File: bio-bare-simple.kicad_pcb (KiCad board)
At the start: 2 copper layers, 49.7 x 49.7 mm, 6 parts, among them X1 Badgelife_shitty_connector

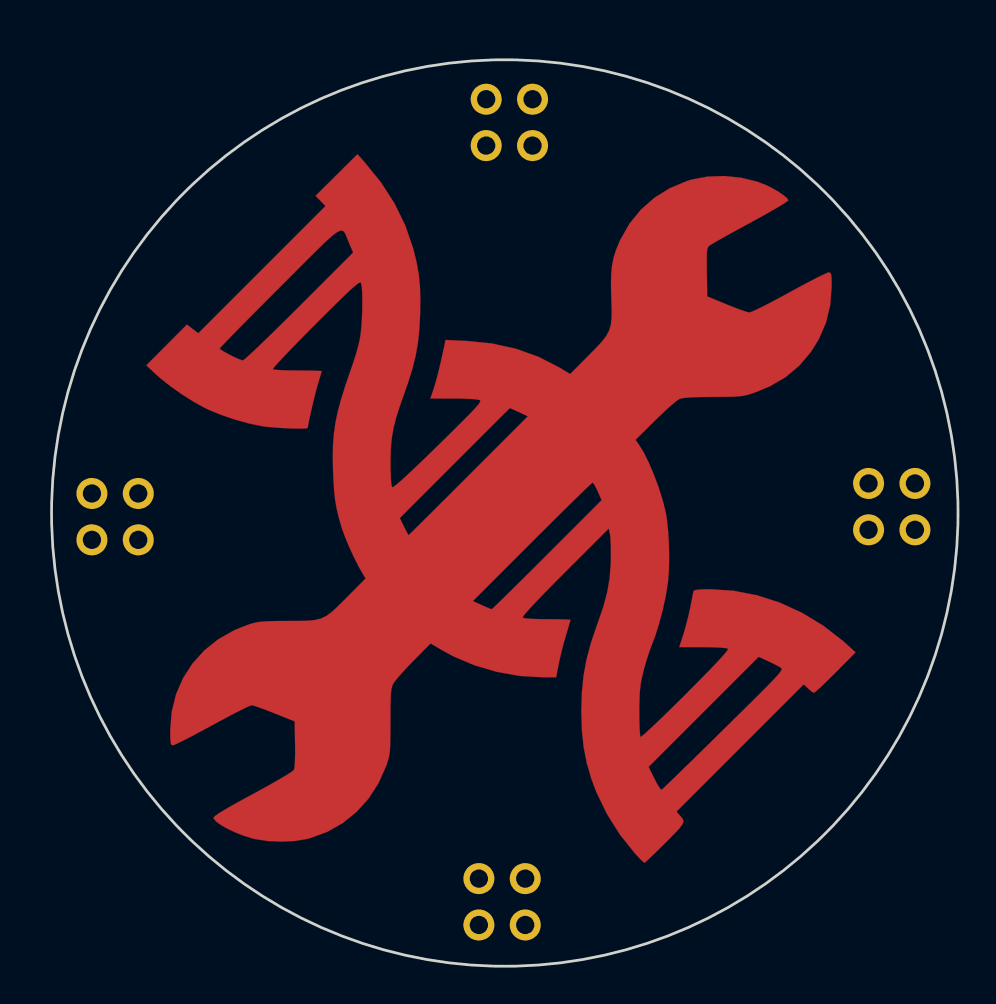
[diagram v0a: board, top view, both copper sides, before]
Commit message: add simple BioHacking Village artwork to add-on board
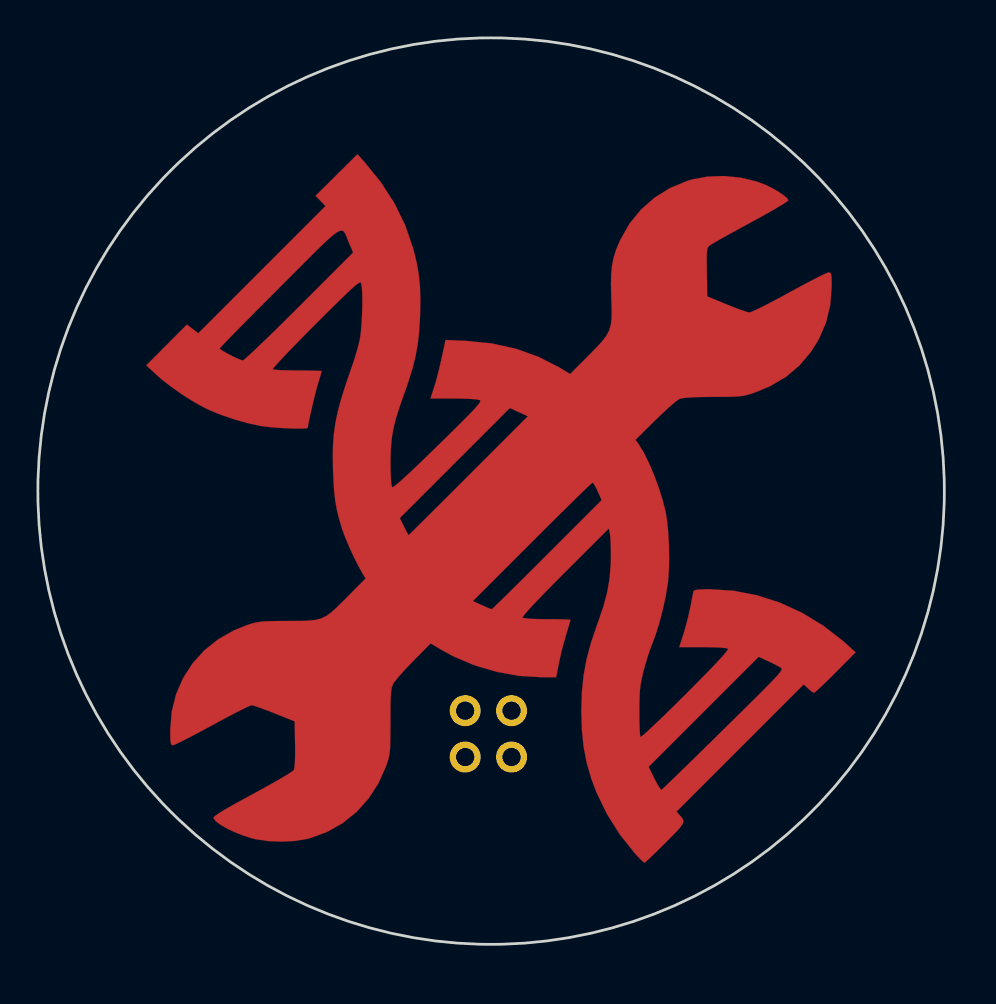
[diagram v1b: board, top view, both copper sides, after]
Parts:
- removed the X1 at (147.3, 135.8)
- removed the X1 at (168.3, 156.8)
- removed the X1 at (125.8, 157.3)
- moved X1 9.23 mm to (146.2, 169.2)
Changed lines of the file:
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@@
 (kicad_pcb (version 4) (host pcbnew 4.0.6+dfsg1-1)
   (general
-    (links 12)
-    (no_connects 12)
+    (links 0)
+    (no_connects 0)
     (area 94.116316 137.286666 171.450001 210.500001)
     (thickness 1.6)
@@
     (tracks 0)
     (zones 0)
-    (modules 6)
+    (modules 3)
     (nets 5)
   )
@@
     (add_net SCL)
     (add_net SDA)
-  )
-  (module mrmeeseeks:Badgelife-Shitty-2x2 (layer B.Cu)
-    (at 147.35 135.75)
-    (descr "Through hole angled pin header, 2x02, 2.54mm pitch, 6mm pin length, double rows")
-    (tags "Through hole angled pin header THT 2x02 2.54mm double row")
-    (fp_text reference X1 (at 0 0) (layer B.Fab)
-      (effects (font (size 1 1) (thickness 0.15)) (justify mirror))
-    )
-    (fp_text value Badgelife_shitty_connector (at 0 -4.2) (layer B.Fab)
-      (effects (font (size 1 1) (thickness 0.15)) (justify mirror))
-    )
-    (fp_line (start -25 -9) (end 25 -9) (layer B.Fab) (width 0.1))
-    (fp_circle (center -2.54 2.54) (end -2.14 2.54) (layer B.SilkS) (width 0.15))
-    (fp_line (start -25 41) (end -25 -9) (layer B.Fab) (width 0.1))
-    (fp_line (start 25 41) (end 25 -9) (layer B.Fab) (width 0.1))
-    (fp_line (start -25 41) (end 25 41) (layer B.Fab) (width 0.1))
-    (pad 4 thru_hole circle (at 1.27 1.27) (size 1.7 1.7) (drill 1) (layers *.Cu *.Mask)
-      (net 3 SDA))
-    (pad 3 thru_hole oval (at 1.27 -1.27) (size 1.7 1.7) (drill 1) (layers *.Cu *.Mask)
-      (net 4 SCL))
-    (pad 1 thru_hole oval (at -1.27 1.27) (size 1.7 1.7) (drill 1) (layers *.Cu *.Mask)
-      (net 1 +3V3))
-    (pad 2 thru_hole oval (at -1.27 -1.27) (size 1.7 1.7) (drill 1) (layers *.Cu *.Mask)
-      (net 2 GND))
-  )
-  (module mrmeeseeks:Badgelife-Shitty-2x2 (layer B.Cu)
-    (at 168.3 156.8)
-    (descr "Through hole angled pin header, 2x02, 2.54mm pitch, 6mm pin length, double rows")
-    (tags "Through hole angled pin header THT 2x02 2.54mm double row")
-    (fp_text reference X1 (at 0 0) (layer B.Fab)
-      (effects (font (size 1 1) (thickness 0.15)) (justify mirror))
-    )
-    (fp_text value Badgelife_shitty_connector (at 0 -4.2) (layer B.Fab)
-      (effects (font (size 1 1) (thickness 0.15)) (justify mirror))
-    )
-    (fp_line (start -25 -9) (end 25 -9) (layer B.Fab) (width 0.1))
-    (fp_circle (center -2.54 2.54) (end -2.14 2.54) (layer B.SilkS) (width 0.15))
-    (fp_line (start -25 41) (end -25 -9) (layer B.Fab) (width 0.1))
-    (fp_line (start 25 41) (end 25 -9) (layer B.Fab) (width 0.1))
-    (fp_line (start -25 41) (end 25 41) (layer B.Fab) (width 0.1))
-    (pad 4 thru_hole circle (at 1.27 1.27) (size 1.7 1.7) (drill 1) (layers *.Cu *.Mask)
-      (net 3 SDA))
-    (pad 3 thru_hole oval (at 1.27 -1.27) (size 1.7 1.7) (drill 1) (layers *.Cu *.Mask)
-      (net 4 SCL))
-    (pad 1 thru_hole oval (at -1.27 1.27) (size 1.7 1.7) (drill 1) (layers *.Cu *.Mask)
-      (net 1 +3V3))
-    (pad 2 thru_hole oval (at -1.27 -1.27) (size 1.7 1.7) (drill 1) (layers *.Cu *.Mask)
-      (net 2 GND))
-  )
-  (module mrmeeseeks:Badgelife-Shitty-2x2 (layer B.Cu)
-    (at 125.75 157.35)
-    (descr "Through hole angled pin header, 2x02, 2.54mm pitch, 6mm pin length, double rows")
-    (tags "Through hole angled pin header THT 2x02 2.54mm double row")
-    (fp_text reference X1 (at 0 0) (layer B.Fab)
-      (effects (font (size 1 1) (thickness 0.15)) (justify mirror))
-    )
-    (fp_text value Badgelife_shitty_connector (at 0 -4.2) (layer B.Fab)
-      (effects (font (size 1 1) (thickness 0.15)) (justify mirror))
-    )
-    (fp_line (start -25 -9) (end 25 -9) (layer B.Fab) (width 0.1))
-    (fp_circle (center -2.54 2.54) (end -2.14 2.54) (layer B.SilkS) (width 0.15))
-    (fp_line (start -25 41) (end -25 -9) (layer B.Fab) (width 0.1))
-    (fp_line (start 25 41) (end 25 -9) (layer B.Fab) (width 0.1))
-    (fp_line (start -25 41) (end 25 41) (layer B.Fab) (width 0.1))
-    (pad 4 thru_hole circle (at 1.27 1.27) (size 1.7 1.7) (drill 1) (layers *.Cu *.Mask)
-      (net 3 SDA))
-    (pad 3 thru_hole oval (at 1.27 -1.27) (size 1.7 1.7) (drill 1) (layers *.Cu *.Mask)
-      (net 4 SCL))
-    (pad 1 thru_hole oval (at -1.27 1.27) (size 1.7 1.7) (drill 1) (layers *.Cu *.Mask)
-      (net 1 +3V3))
-    (pad 2 thru_hole oval (at -1.27 -1.27) (size 1.7 1.7) (drill 1) (layers *.Cu *.Mask)
-      (net 2 GND))
   )
   (module badgelife_dev_board:wrench-neg-mask (layer F.Cu)
@@
   )
   (module mrmeeseeks:Badgelife-Shitty-2x2 (layer B.Cu)
-    (at 146.95 178.45)
+    (at 146.2 169.25)
     (descr "Through hole angled pin header, 2x02, 2.54mm pitch, 6mm pin length, double rows")
     (tags "Through hole angled pin header THT 2x02 2.54mm double row")
@@
       (xy -8.446472 -17.547497) (xy -8.717854 -17.827493) (xy -6.422394 -20.108333) (xy -6.042095 -19.685)) (layer F.Cu) (width 0.01))
   )
-  (gr_circle (center 147.1 157.15) (end 137.5 134.25) (layer Edge.Cuts) (width 0.15))
+  (gr_circle (center 146.35 155.95) (end 136.75 133.05) (layer Edge.Cuts) (width 0.15))
   (dimension 6.500769 (width 0.3) (layer Dwgs.User)
     (gr_text "6.501 mm" (at 99.902029 145.192277 270.881404) (layer Dwgs.User)
